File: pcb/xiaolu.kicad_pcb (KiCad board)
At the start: 2 copper layers, 51 x 76 mm, 39 parts, among them J1 Conn_01x04_Male, J2 TRRS, SW1 SW_Push, SW10 SW_Push, SW11 SW_Push, SW12 SW_Push, SW13 SW_Push, SW14 SW_Push, SW15 SW_Push, SW16 SW_Push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

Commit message: add slikscreen logos and label
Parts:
- added REF**5: cat_in_136_inversed_2.54mm_SilkScreen, Xiaolu-Specific:cat_in_136_inversed_2.54mm_SilkScreen, B.Cu at (75.5, 118.8)
- added REF**6: Symbol_CreativeCommons_CC-BY-SA_SilkScreen, Xiaolu-Specific:Symbol_CreativeCommons_CC-BY-SA_SilkScreen, B.Cu at (71.4, 118.5)
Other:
- board text added: "@cat_in_136/CC BY-SA"
- board text added: "Xiaolu KBD v${REVISION}"

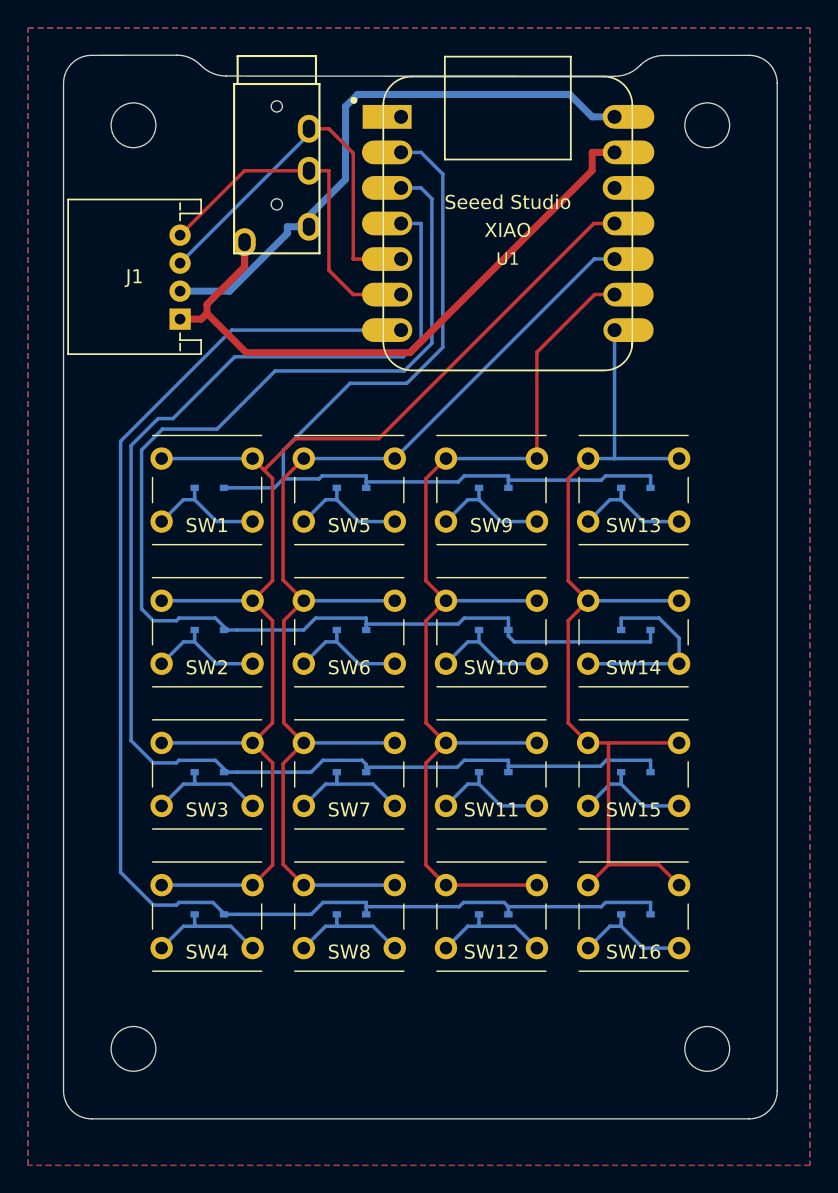
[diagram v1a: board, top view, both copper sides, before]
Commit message: fix Grove connector
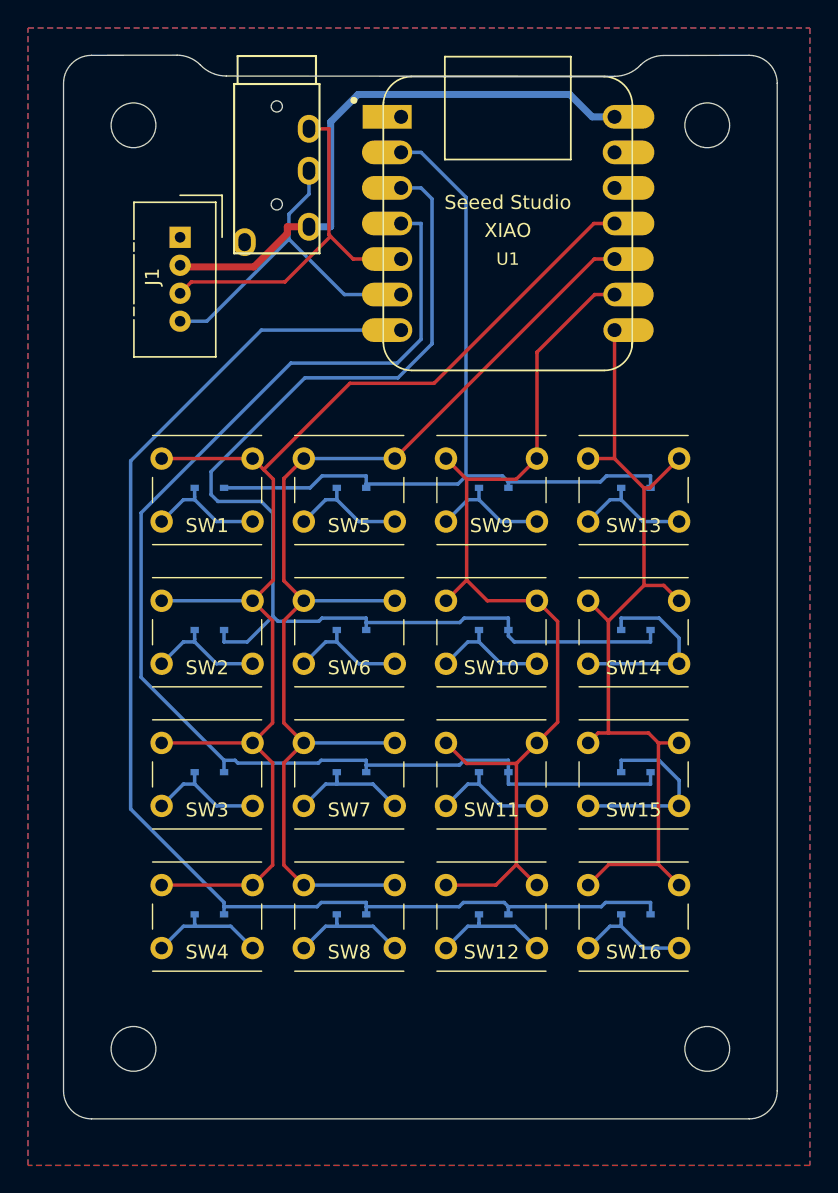
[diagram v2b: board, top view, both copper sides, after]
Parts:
- J1: footprint Xiaolu-Specific:NS-Tech_Grove_1x04_P2mm_Horizontal -> Connector:NS-Tech_Grove_1x04_P2mm_Vertical
- moved J1 5.85 mm to (59.1, 63.2), turned to 0 degrees
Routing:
- net GND: track 45.3 -> 0.00 mm
- net row1: track 89.2 -> 82.0 mm
- net row0: track 66.2 -> 59.4 mm
- net row2: track 96.2 -> 90.0 mm
- net Net-(D15-Pad2): track 8.64 -> 13.9 mm
- net row3: track 96.4 -> 91.6 mm
- net col2: track 74.9 -> 71.5 mm
- net col3: track 67.8 -> 64.5 mm
- net SDA: track 28.3 -> 27.3 mm

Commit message: add I2C pin layout label
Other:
- board text added: "GND 5V SDA/GP6 SCL/GP7"
- board text added: "R2:SDA R1:SCL T:5V S:GND"
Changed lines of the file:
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@@
     (effects (font (size 1 1) (thickness 0.15)) (justify right mirror))
+  )
+  (gr_text "GND\n5V\nSDA/GP6\nSCL/GP7" (at 57.785 66.04) (layer "B.SilkS")
+    (effects (font (size 0.8 0.8) (thickness 0.15)) (justify left mirror))
+  )
+  (gr_text "R2:SDA\nR1:SCL\nT:5V\nS:GND" (at 65.405 57.3767) (layer "B.SilkS")
+    (effects (font (size 0.8 0.8) (thickness 0.15)) (justify left mirror))
   )
   (dimension (type aligned) (layer "Eco1.User")

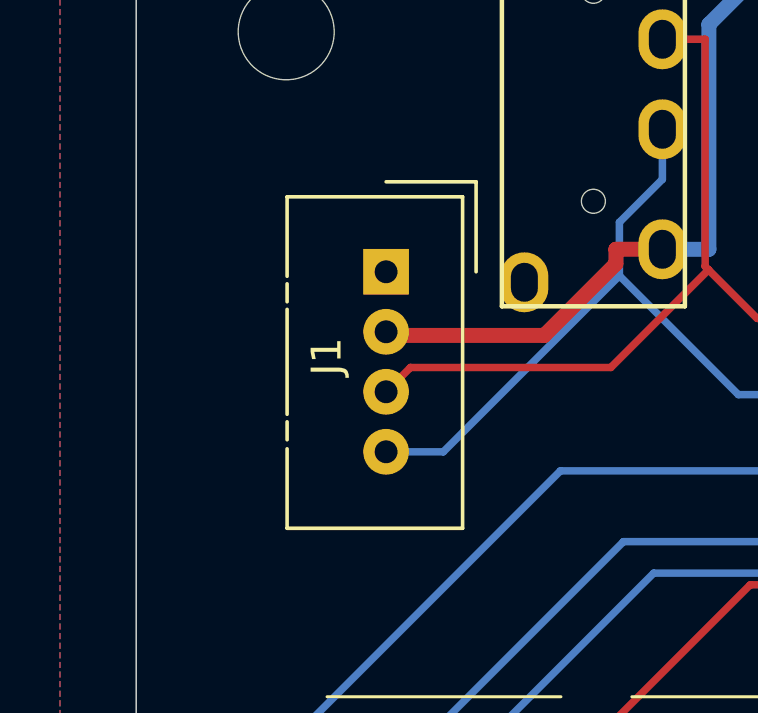
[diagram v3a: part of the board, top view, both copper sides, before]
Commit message: use NS-Tech_Grove_1x04_P2mm_Hybrid.kicad_mod for grove connector footprint and fix the Grove connector position
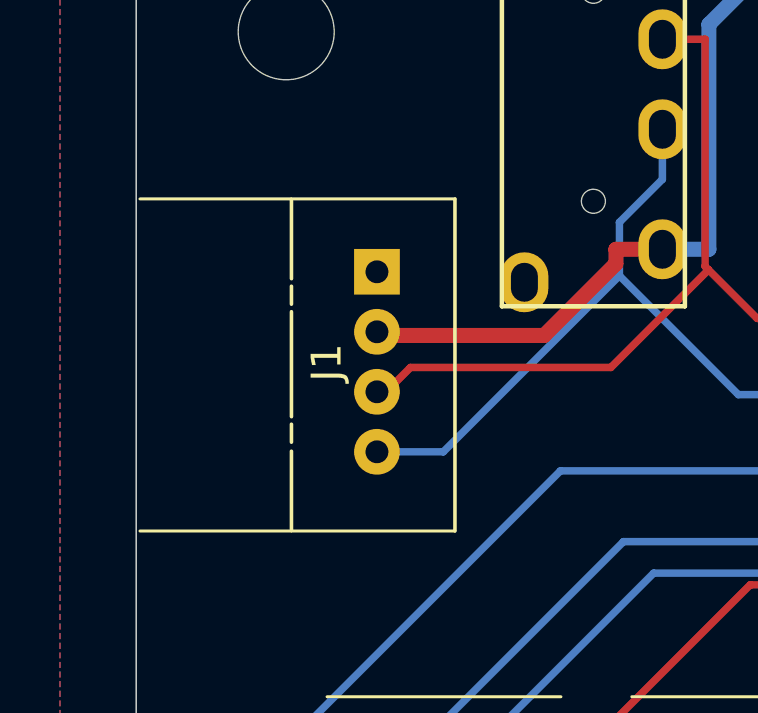
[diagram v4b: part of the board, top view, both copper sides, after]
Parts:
- J1: footprint Connector:NS-Tech_Grove_1x04_P2mm_Vertical -> Xiaolu-Specific:NS-Tech_Grove_1x04_P2mm_Hybrid
- moved J1 0.30 mm to (58.8, 63.2)
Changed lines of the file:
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@@
       (net 22 "+5V") (pinfunction "5V") (pintype "power_in"))
   )
-  (footprint "Connector:NS-Tech_Grove_1x04_P2mm_Vertical" (layer "F.Cu")
-    (at 59.13 63.215)
+  (footprint "Xiaolu-Specific:NS-Tech_Grove_1x04_P2mm_Hybrid" (layer "F.Cu")
+    (at 58.825 63.215)
     (descr "https://statics3.seeedstudio.com/images/opl/datasheet/3470130P1.pdf")
     (tags "Grove-1x04")
@@
     (property "Sheetname" "")
     (attr through_hole)
-    (fp_text reference "J1" (at -1.98 2.825 90) (layer "F.SilkS")
+    (fp_text reference "J1" (at -1.675 3.025 90) (layer "F.SilkS")
       (effects (font (size 1 1) (thickness 0.15)))
     )
@@
       (effects (font (size 1 1) (thickness 0.15)))
     )
-    (fp_line (start 0 -3) (end 3 -3) (layer "F.SilkS") (width 0.12))
-    (fp_line (start -3.3 1.25) (end -3.3 4.75) (layer "F.SilkS") (width 0.12))
-    (fp_line (start -3.3 8.55) (end 2.55 8.55) (layer "F.SilkS") (width 0.12))
-    (fp_line (start -3.3 -2.5) (end -3.3 0.15) (layer "F.SilkS") (width 0.12))
-    (fp_line (start -3.3 0.4) (end -3.3 1) (layer "F.SilkS") (width 0.12))
-    (fp_line (start -3.3 -2.5) (end 2.55 -2.5) (layer "F.SilkS") (width 0.12))
-    (fp_line (start 3 -3) (end 3 0) (layer "F.SilkS") (width 0.12))
-    (fp_line (start -3.3 5.9) (end -3.3 8.55) (layer "F.SilkS") (width 0.12))
-    (fp_line (start -3.3 5) (end -3.3 5.6) (layer "F.SilkS") (width 0.12))
-    (fp_line (start 2.55 -2.5) (end 2.55 8.55) (layer "F.SilkS") (width 0.12))
+    (fp_line (start -2.85 5.08) (end -2.85 5.68) (layer "F.SilkS") (width 0.12))
+    (fp_line (start -2.85 5.98) (end -2.85 8.63) (layer "F.SilkS") (width 0.12))
+    (fp_line (start 2.6 -2.43) (end 2.6 8.64) (layer "F.SilkS") (width 0.12))
+    (fp_line (start -2.85 1.33) (end -2.85 4.83) (layer "F.SilkS") (width 0.12))
+    (fp_line (start 2.6 8.64) (end -7.9 8.64) (layer "F.SilkS") (width 0.1))
+    (fp_line (start -2.85 -2.42) (end -2.85 0.23) (layer "F.SilkS") (width 0.12))
+    (fp_line (start -2.85 0.48) (end -2.85 1.08) (layer "F.SilkS") (width 0.12))
+    (fp_line (start -7.9 -2.43) (end 2.6 -2.43) (layer "F.SilkS") (width 0.1))
+    (fp_line (start -8 -2.65) (end -8 8.7) (layer "F.CrtYd") (width 0.05))
     (fp_line (start 2.7 8.7) (end 2.7 -2.65) (layer "F.CrtYd") (width 0.05))
-    (fp_line (start -3.45 8.7) (end 2.7 8.7) (layer "F.CrtYd") (width 0.05))
-    (fp_line (start -3.45 -2.65) (end 2.7 -2.65) (layer "F.CrtYd") (width 0.05))
-    (fp_line (start -3.45 -2.65) (end -3.45 8.7) (layer "F.CrtYd") (width 0.05))
+    (fp_line (start -8 -2.65) (end 2.7 -2.65) (layer "F.CrtYd") (width 0.05))
+    (fp_line (start -8 8.7) (end 2.7 8.7) (layer "F.CrtYd") (width 0.05))
+    (fp_line (start 0 7.51) (end 1.5 7.51) (layer "F.Fab") (width 0.12))
     (fp_line (start -2.9 8.1) (end -2.9 -2.1) (layer "F.Fab") (width 0.1))
-    (fp_line (start -2.9 -2.1) (end 2.2 -2.1) (layer "F.Fab") (width 0.1))
+    (fp_line (start 1.5 -1.51) (end 1.5 -2.1) (layer "F.Fab") (width 0.12))
     (fp_line (start 2.2 -2.1) (end 2.2 8.1) (layer "F.Fab") (width 0.1))
-    (fp_line (start 2.2 -1) (end 0.9 0) (layer "F.Fab") (width 0.1))
     (fp_line (start 0.9 0) (end 2.2 1) (layer "F.Fab") (width 0.1))
-    (fp_line (start 2.2 8.1) (end -2.9 8.1) (layer "F.Fab") (width 0.1))
+    (fp_line (start -8 8.1) (end -8 -2.1) (layer "F.Fab") (width 0.1))
+    (fp_line (start 1.5 -1.51) (end 0 -1.51) (layer "F.Fab") (width 0.12))
+    (fp_line (start 1.5 8.1) (end 1.5 7.51) (layer "F.Fab") (width 0.12))
+    (fp_line (start 2.2 -1) (end 0.9 0) (layer "F.Fab") (width 0.1))
+    (fp_line (start -8 -2.1) (end 2.2 -2.1) (layer "F.Fab") (width 0.1))
+    (fp_line (start 2.2 8.1) (end -8 8.1) (layer "F.Fab") (width 0.1))
+    (fp_line (start 0 -1.51) (end 0 7.51) (layer "F.Fab") (width 0.1))
     (pad "1" thru_hole rect (at 0 0) (size 1.524 1.524) (drill 0.762) (layers *.Cu *.Mask)
       (net 21 "GND") (pinfunction "Pin_1") (pintype "passive"))
@@
     (pad "4" thru_hole circle (at 0 6) (size 1.524 1.524) (drill 0.762) (layers *.Cu *.Mask)
       (net 24 "SCL") (pinfunction "Pin_4") (pintype "passive"))
-    (model "${KICAD6_3DMODEL_DIR}/Connector.3dshapes/NS-Tech_Grove_1x04_P2mm_Vertical.wrl"
-      (offset (xyz 0 0 0))
+    (model "${KIPRJMOD}/libfootprints.pretty/3dmodels/Grove_Connector.wrl"
+      (offset (xyz 0 -6 0))
       (scale (xyz 0.3937 0.3937 0.3937))
-      (rotate (xyz 0 0 -90))
+      (rotate (xyz 0 0 180))
     )
   )
@@
   (gr_line (start 90.17 51.714214) (end 62.43 51.693144) (layer "Edge.Cuts") (width 0.05))
   (gr_line (start 58.911758 50.203679) (end 52.8 50.214214) (layer "Edge.Cuts") (width 0.05))
-  (gr_text "@cat_in_136/CC BY-SA" (at 60.96 123.19) (layer "B.SilkS")
-    (effects (font (size 0.8 0.8) (thickness 0.15)) (justify right mirror))
-  )
   (gr_text "Xiaolu KBD v${REVISION}" (at 80.01 121.2142) (layer "B.SilkS")
     (effects (font (size 1 1) (thickness 0.15)) (justify right mirror))
   )
-  (gr_text "GND\n5V\nSDA/GP6\nSCL/GP7" (at 57.785 66.04) (layer "B.SilkS")
+  (gr_text "@cat_in_136/CC BY-SA" (at 60.96 123.19) (layer "B.SilkS")
+    (effects (font (size 0.8 0.8) (thickness 0.15)) (justify right mirror))
+  )
+  (gr_text "GND\n5V\nSDA/GP6\nSCL/GP7" (at 57.15 66.04) (layer "B.SilkS")
     (effects (font (size 0.8 0.8) (thickness 0.15)) (justify left mirror))
   )

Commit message: fix SDA/SCL pin numbers of I2C pin layout label
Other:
- board text added: "GND 5V SDA/GP5 SCL/GP6"
- board text removed: "GND 5V SDA/GP6 SCL/GP7"
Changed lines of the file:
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@@
     (effects (font (size 0.8 0.8) (thickness 0.15)) (justify right mirror))
   )
-  (gr_text "GND\n5V\nSDA/GP6\nSCL/GP7" (at 57.15 66.04) (layer "B.SilkS")
+  (gr_text "GND\n5V\nSDA/GP5\nSCL/GP6" (at 57.15 66.04) (layer "B.SilkS")
     (effects (font (size 0.8 0.8) (thickness 0.15)) (justify left mirror))
   )
